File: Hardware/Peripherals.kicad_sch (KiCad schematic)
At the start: 21 parts, among them J3 0532610271, J5 B8B-PH-SM4-TB, J6 0532610671, U4 DRV2605LDGS, U5 BNO055, U6 M20048-1

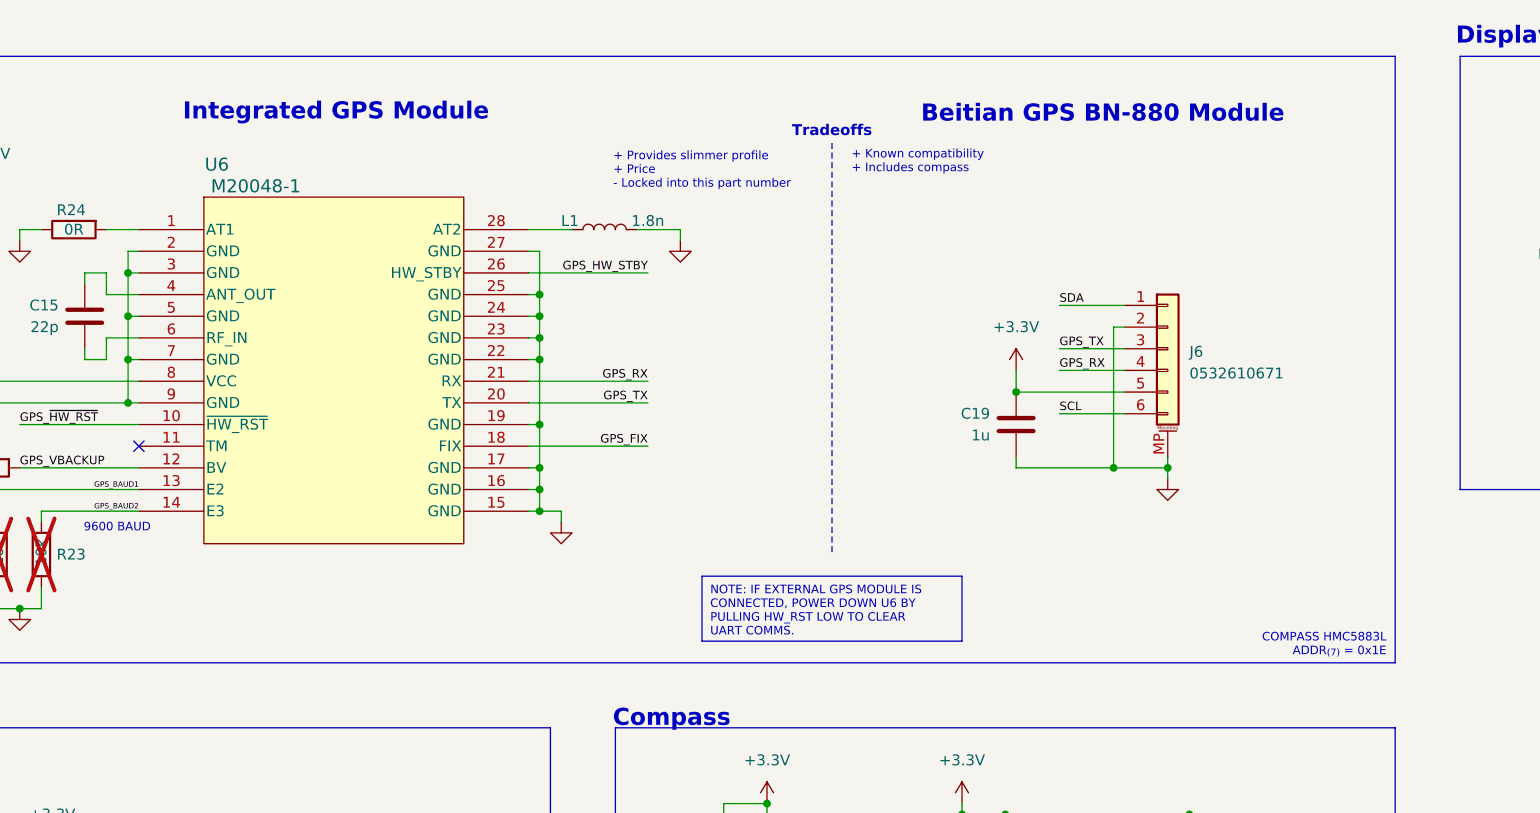
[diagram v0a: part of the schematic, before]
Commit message: update board outline and flip 180
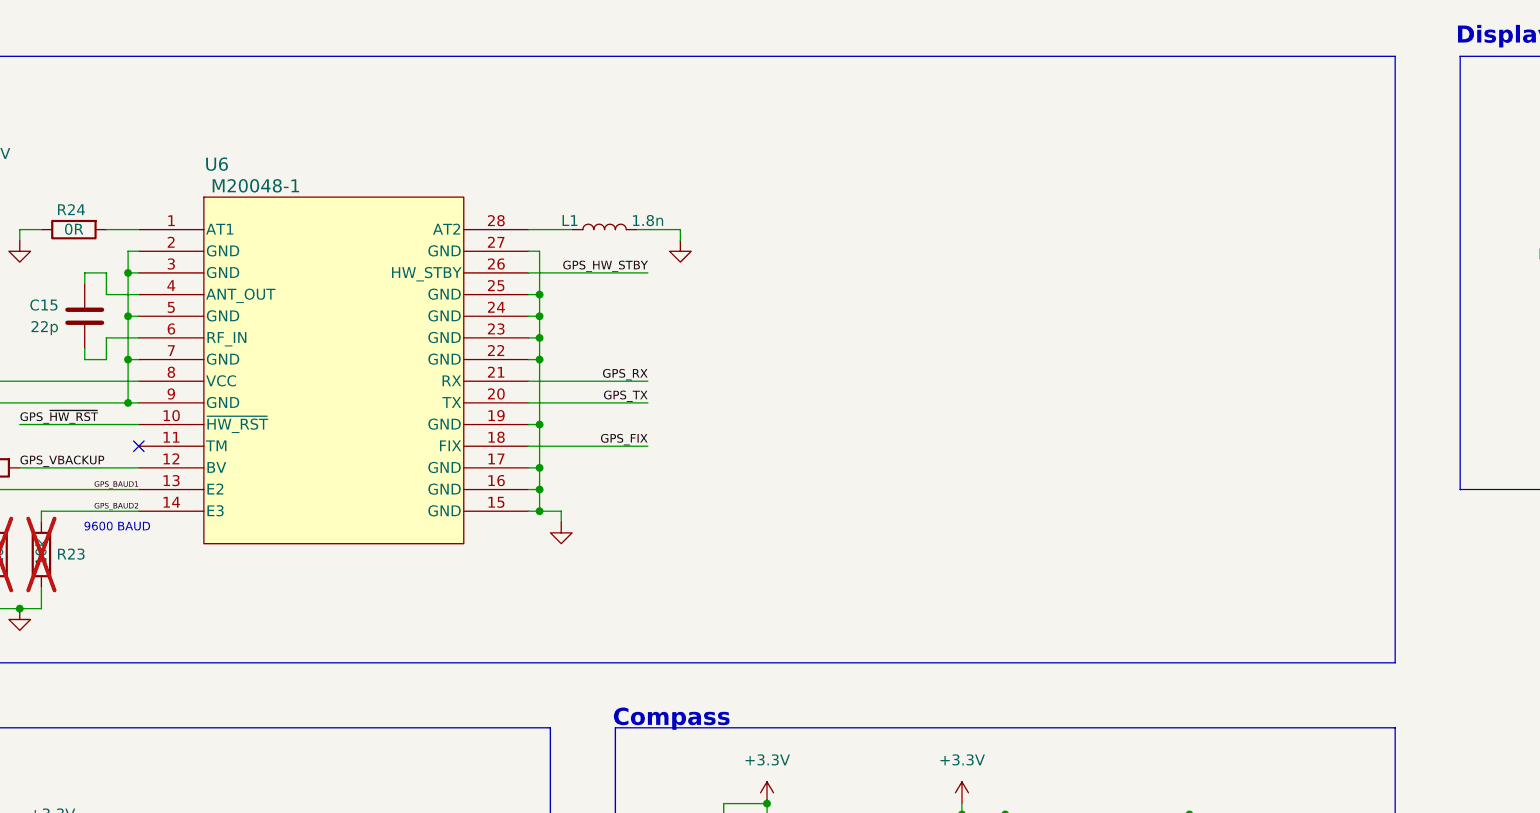
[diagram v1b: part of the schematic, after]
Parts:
- removed C19: 1u, Capacitor_SMD:C_0603_1608Metric, symbol Device:C
- removed J6: 0532610671, Connector_Molex:Molex_PicoBlade_53261-0671_1x06-1MP_P1.25mm_Horizontal, symbol Connector_Generic_MountingPin:Conn_01x06_MountingPin
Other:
- note removed: "+ Known compatibility + Includes compass"
- note removed: "+ Provides slimmer profile + Price - Locked into this part number"
- note removed: "Beitian GPS BN-880 Module"
- note removed: "COMPASS HMC5883L ADDR_{(7)} = 0x1E"
- note removed: "Integrated GPS Module"
- note removed: "Tradeoffs"

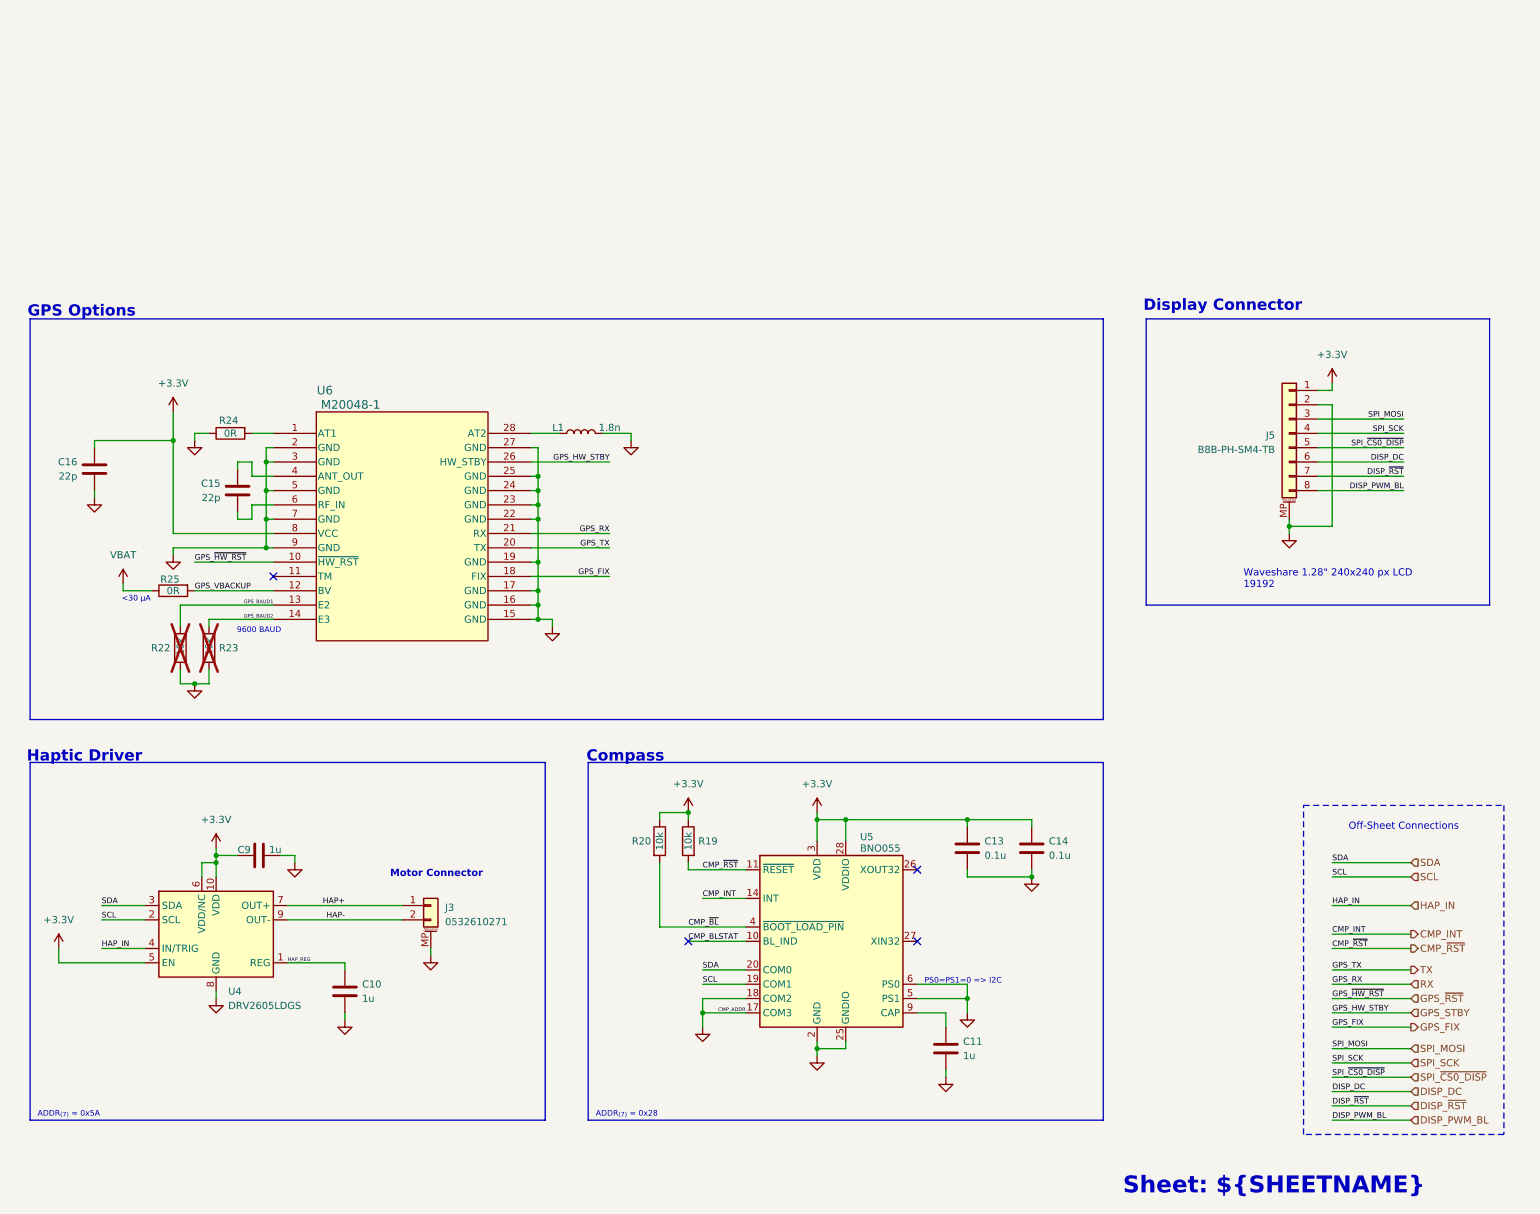
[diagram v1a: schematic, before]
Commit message: sch: replace gps for TESSO-LIV3R
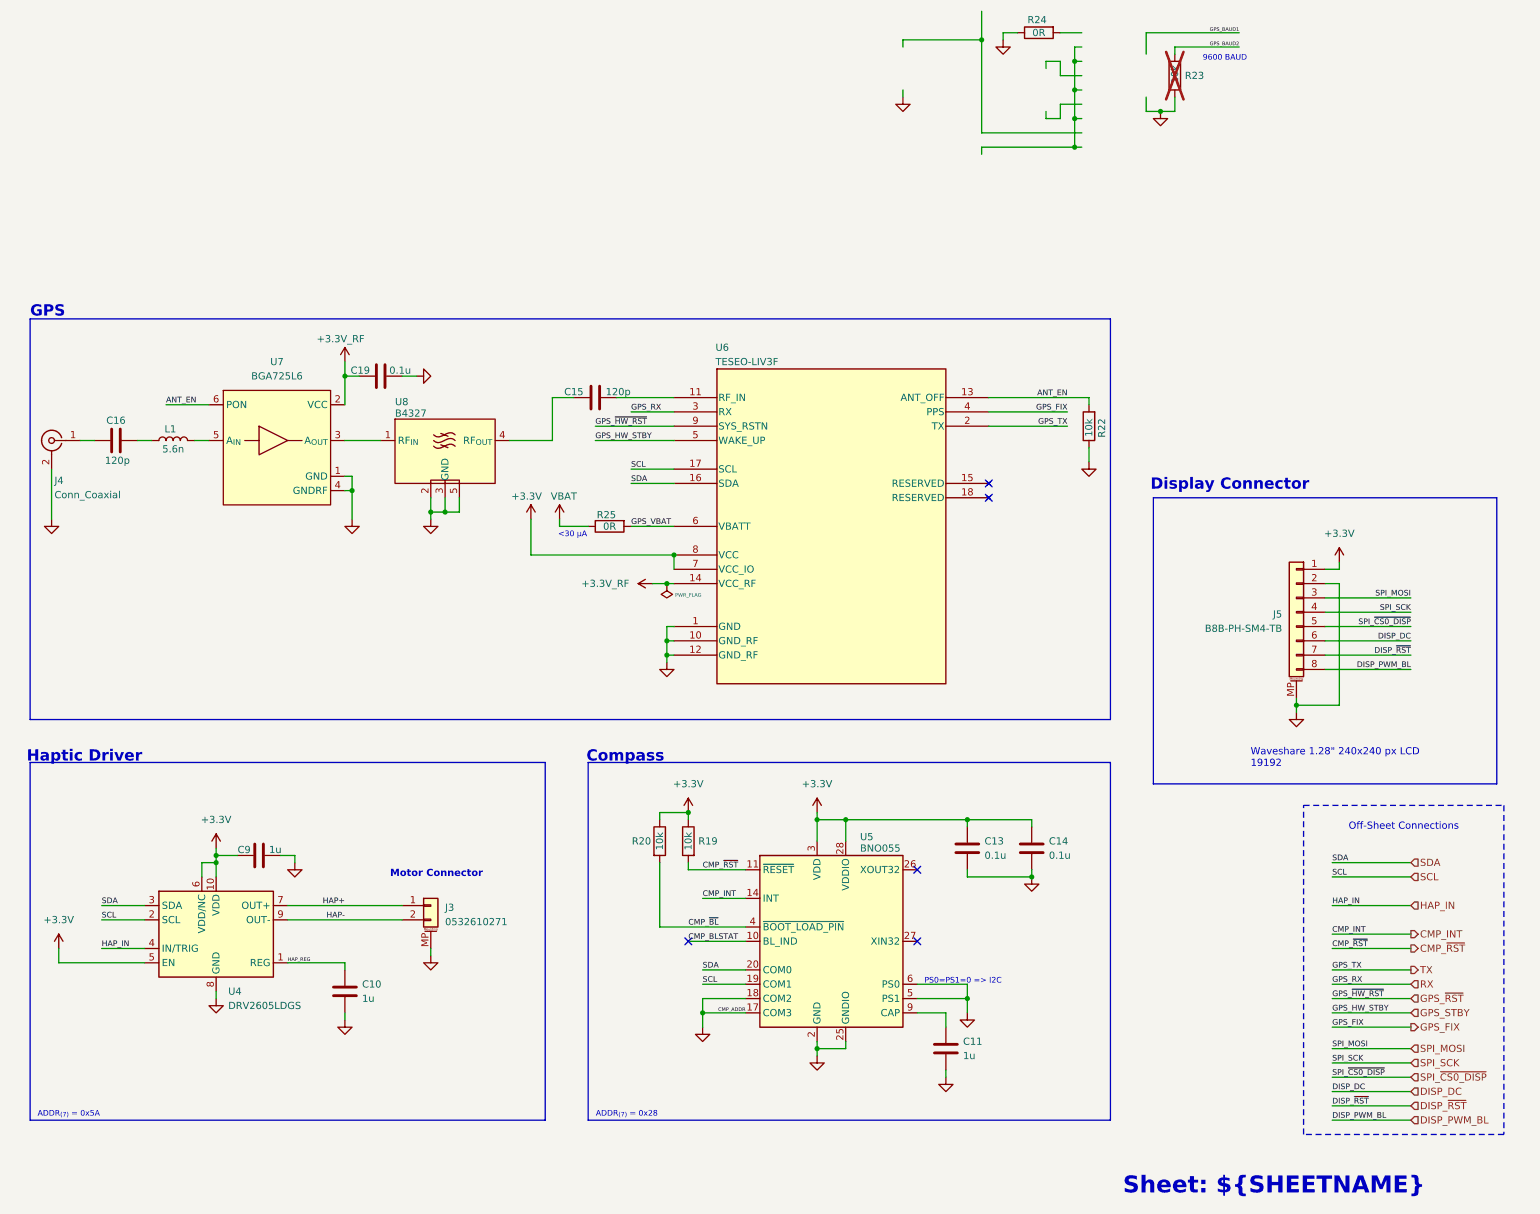
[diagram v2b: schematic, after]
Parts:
- removed U6: M20048-1, M20048-1:QFN28_M20048-1_ANT, symbol 2025-03-22_21-29-02:M20048-1
- added C19: 0.1u, Capacitor_SMD:C_0603_1608Metric, symbol Device:C
- added J4: Conn_Coaxial, Connector_Coaxial:U.FL_Molex_MCRF_73412-0110_Vertical, symbol Connector:Conn_Coaxial
- added U6: TESEO-LIV3F, LCC-18_9P7X10P1_STM, symbol 2025-06-15_18-00-59:TESEO-LIV3F
- added U7: BGA725L6, Symbols:BGA-6_2x3_0.8x1.2mm, symbol 2025-06-15_18-00-59:BGA725L6
- added U8: B4327, Symbols:SOIC-5 B4327, symbol 2025-06-15_18-00-59:B4327
- C15, C16: value 22p -> 120p; footprint Capacitor_SMD:C_0603_1608Metric -> Capacitor_SMD:C_0402_1005Metric; MPN CL10C220JB8NNNC -> GRM1555C2A121GE01D
- L1: value 1.8n -> 5.6n; Alt1 BSCH001608081N8S00 -> (none); MPN LQG18HN1N8S00D -> LQW15AN5N6C10D
- R22: now fitted
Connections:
- net +3.3V: now also U6.7 (VCC_IO), U6.8 (VCC); no longer C16.1
- net GND: now also R22.1, C19.2, J4.2 (Ext), U6.1 (GND), U6.10 (GND_RF), U6.12 (GND_RF), U7.1 (GND), U7.4 (GNDRF), U8.2, U8.3 (GND), U8.5; no longer C16.2, L1.2, R22.2
- net GPS_BAUD1: no longer R22.1
- net GPS_FIX: now also U6.4 (PPS)
- net GPS_STBY: now also U6.5 (WAKE_UP)
- net GPS_~{RST}: now also U6.9 (SYS_RSTN)
- net RX: now also U6.3 (RX)
- net SCL: now also U6.17 (SCL)
- net SDA: now also U6.16 (SDA)
- net TX: now also U6.2 (TX)
- net at C15.1: now also U6.11 (RF_IN)
- net at C15.2: now also U8.4 (RF_{OUT})
- net at L1.1: now also C16.1
- net GPS_VBACKUP renamed GPS_VBAT
- net GPS_VBAT: now also U6.6 (VBATT)
- new net: C16.2, J4.1 (In)
- new net: L1.2, U7.5 (A_{IN})
- new net: U7.3 (A_{OUT}), U8.1 (RF_{IN})
- new net +3.3V_RF: C19.1, U6.14 (VCC_RF), U7.2 (VCC)
- new net ANT_EN: R22.2, U6.13 (ANT_OFF), U7.6 (PON)
- no-connect marks 4 -> 5
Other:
- note added: "GPS"
- note removed: "GPS Options"
- moved on the sheet: C16, J5, L1, R23, R24, R25

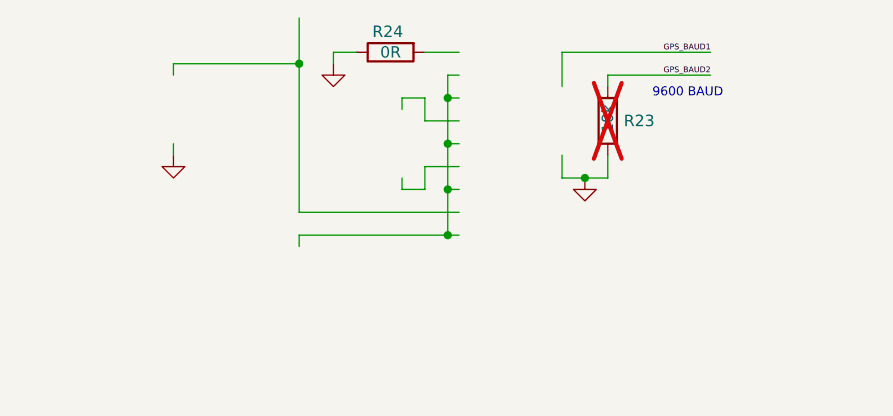
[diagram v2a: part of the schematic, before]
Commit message: pcb: initial layout of TESSO gps
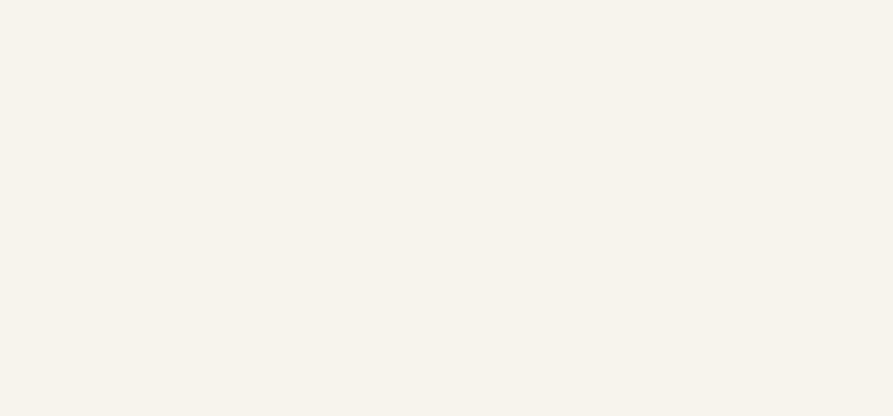
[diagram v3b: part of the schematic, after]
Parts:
- removed R23: 10k, Resistor_SMD:R_0603_1608Metric, symbol Device:R
- removed R24: 0R, Resistor_SMD:R_0603_1608Metric, symbol Device:R
- L1: footprint Inductor_SMD:L_0603_1608Metric -> Inductor_SMD:L_0402_1005Metric
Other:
- note removed: "9600 BAUD"
